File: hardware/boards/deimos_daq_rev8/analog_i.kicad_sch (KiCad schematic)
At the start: 1 part

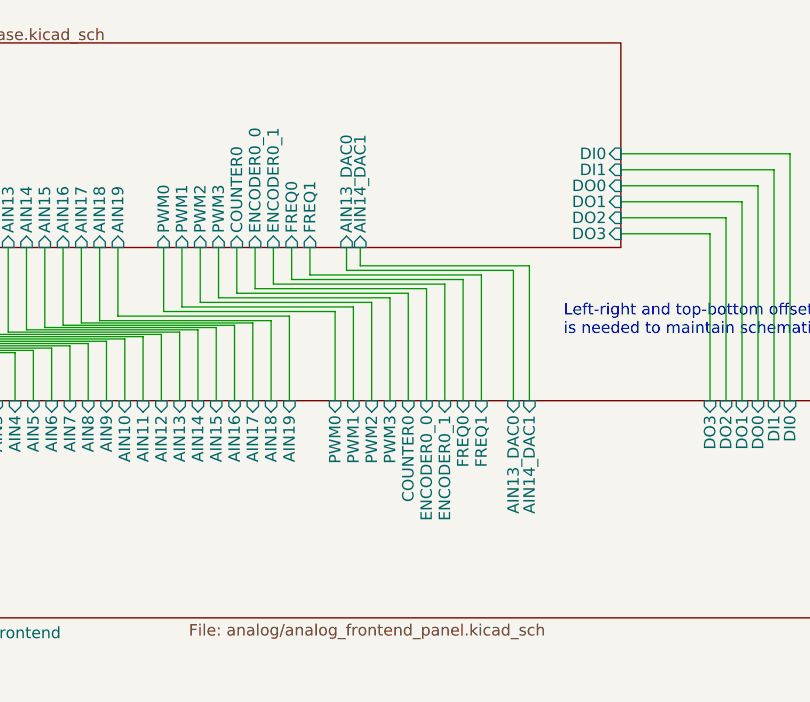
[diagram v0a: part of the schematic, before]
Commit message: update gpio input buffer schematic to use 22k resistor and schottky to 3v3 instead of zener to ground
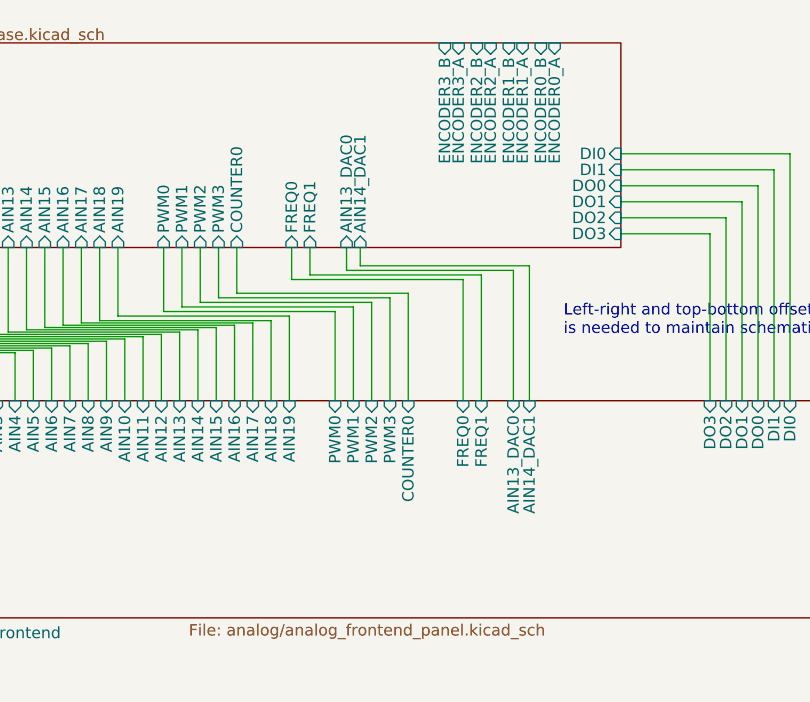
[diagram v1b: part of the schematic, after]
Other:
- sheet analog_frontend ports: added none; removed ENCODER0_0, ENCODER0_1
- sheet base ports: added ENCODER0_A, ENCODER0_B, ENCODER1_A, ENCODER1_B, ENCODER2_A, ENCODER2_B, ENCODER3_A, ENCODER3_B; removed ENCODER0_0, ENCODER0_1
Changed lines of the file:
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@@
-	(wire
-		(pts
-			(xy 71.12 39.37) (xy 71.12 43.434)
-		)
-		(stroke
-			(width 0)
-			(type default)
-		)
-	)
 	(wire
 		(pts
@@
 	(wire
 		(pts
-			(xy 71.12 43.434) (xy 90.17 43.434)
-		)
-		(stroke
-			(width 0)
-			(type default)
-		)
-	)
-	(wire
-		(pts
 			(xy 80.772 39.37) (xy 80.772 41.402)
 		)
@@
 	(wire
 		(pts
-			(xy 88.138 56.388) (xy 88.138 43.942)
-		)
-		(stroke
-			(width 0)
-			(type default)
-		)
-	)
-	(wire
-		(pts
 			(xy 77.978 56.388) (xy 77.978 46.482)
 		)
@@
 	(wire
 		(pts
-			(xy 69.088 43.942) (xy 69.088 39.37)
-		)
-		(stroke
-			(width 0)
-			(type default)
-		)
-	)
-	(wire
-		(pts
 			(xy 77.978 46.482) (xy 58.928 46.482)
 		)
@@
 	(wire
 		(pts
-			(xy 90.17 43.434) (xy 90.17 56.388)
-		)
-		(stroke
-			(width 0)
-			(type default)
-		)
-	)
-	(wire
-		(pts
 			(xy 47.752 48.006) (xy 66.802 48.006)
 		)
@@
 		(pts
 			(xy 99.568 41.402) (xy 99.568 56.388)
-		)
-		(stroke
-			(width 0)
-			(type default)
-		)
-	)
-	(wire
-		(pts
-			(xy 88.138 43.942) (xy 69.088 43.942)
 		)
 		(stroke
@@
 			)
 		)
-		(pin "ENCODER0_0" input
-			(at 69.088 39.37 270)
-			(effects
-				(font
-					(size 1.27 1.27)
-				)
-				(justify left)
-			)
-		)
-		(pin "ENCODER0_1" input
-			(at 71.12 39.37 270)
-			(effects
-				(font
-					(size 1.27 1.27)
-				)
-				(justify left)
-			)
-		)
 		(pin "FREQ0" input
 			(at 73.152 39.37 270)
@@
 		(pin "DO0" input
 			(at 109.728 32.512 0)
+			(effects
+				(font
+					(size 1.27 1.27)
+				)
+				(justify right)
+			)
+		)
+		(pin "ENCODER3_A" input
+			(at 91.694 16.637 90)
+			(effects
+				(font
+					(size 1.27 1.27)
+				)
+				(justify right)
+			)
+		)
+		(pin "ENCODER3_B" input
+			(at 90.17 16.637 90)
+			(effects
+				(font
+					(size 1.27 1.27)
+				)
+				(justify right)
+			)
+		)
+		(pin "ENCODER2_B" input
+			(at 93.726 16.637 90)
+			(effects
+				(font
+					(size 1.27 1.27)
+				)
+				(justify right)
+			)
+		)
+		(pin "ENCODER0_B" input
+			(at 100.838 16.637 90)
+			(effects
+				(font
+					(size 1.27 1.27)
+				)
+				(justify right)
+			)
+		)
+		(pin "ENCODER2_A" input
+			(at 95.25 16.637 90)
+			(effects
+				(font
+					(size 1.27 1.27)
+				)
+				(justify right)
+			)
+		)
+		(pin "ENCODER0_A" input
+			(at 102.362 16.637 90)
+			(effects
+				(font
+					(size 1.27 1.27)
+				)
+				(justify right)
+			)
+		)
+		(pin "ENCODER1_A" input
+			(at 98.806 16.637 90)
+			(effects
+				(font
+					(size 1.27 1.27)
+				)
+				(justify right)
+			)
+		)
+		(pin "ENCODER1_B" input
+			(at 97.282 16.637 90)
 			(effects
 				(font
@@
 			)
 		)
-		(pin "ENCODER0_0" input
-			(at 88.138 56.388 90)
-			(effects
-				(font
-					(size 1.27 1.27)
-				)
-				(justify right)
-			)
-		)
 		(pin "FREQ1" input
 			(at 94.234 56.388 90)
 			(effects
 				(font
-					(size 1.27 1.27)
-				)
-				(justify right)
-			)
-		)
-		(pin "ENCODER0_1" input
-			(at 90.17 56.388 90)
-			(effects
-				(font

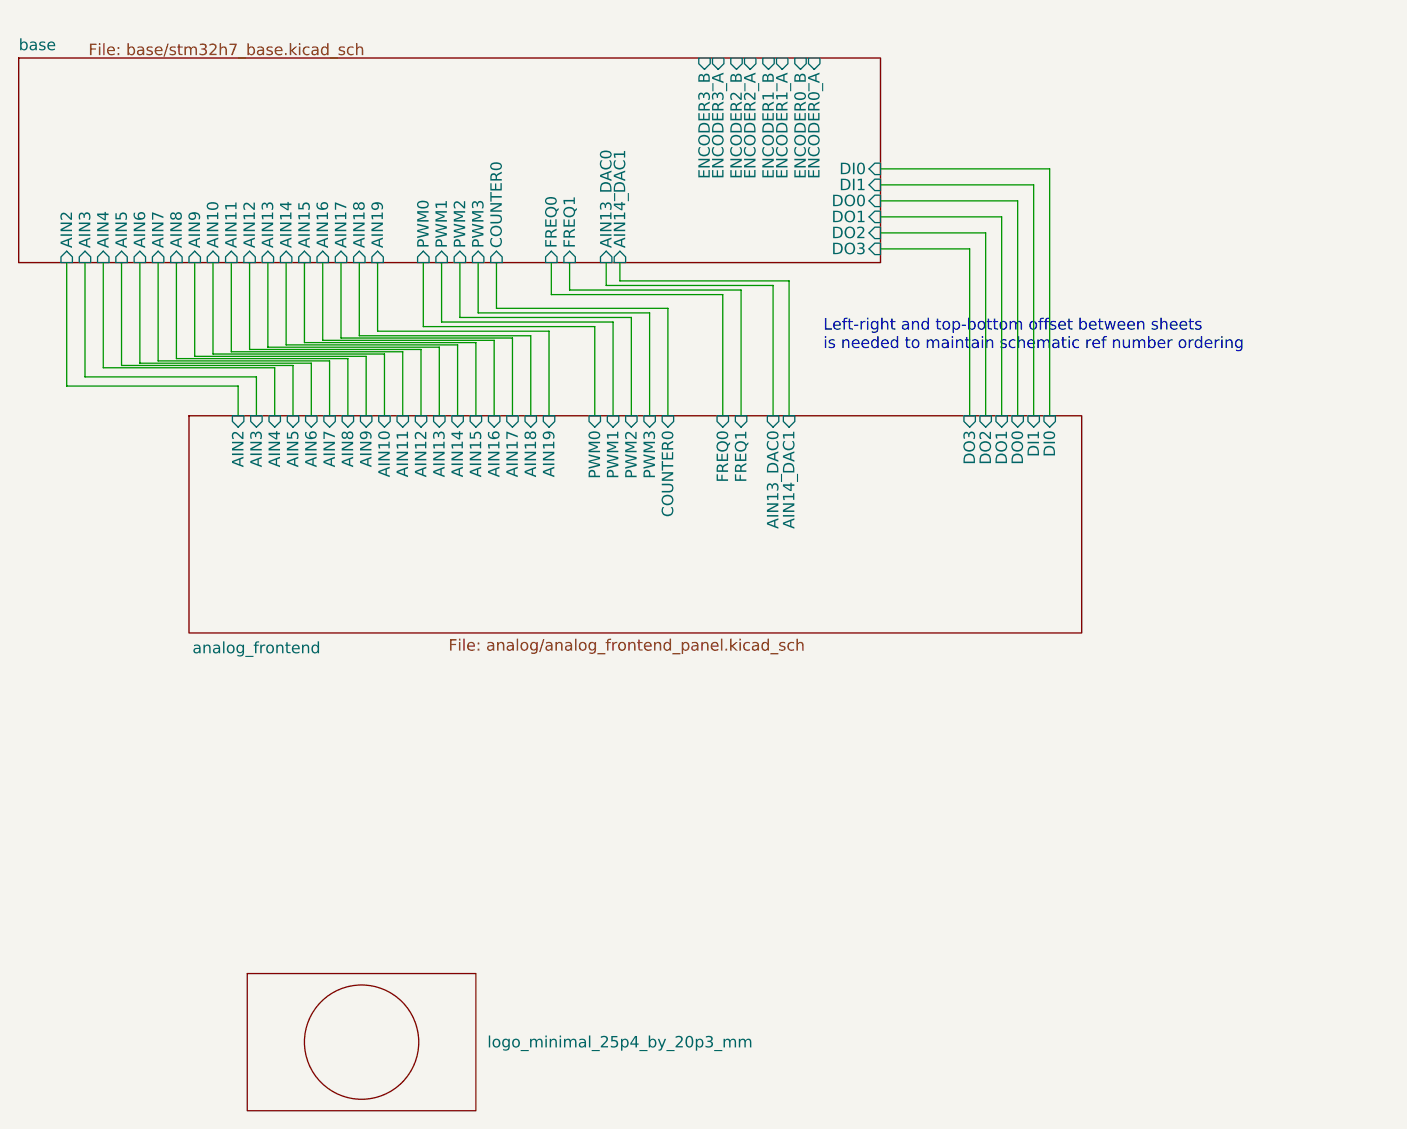
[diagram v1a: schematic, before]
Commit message: finish layout and generate fab files
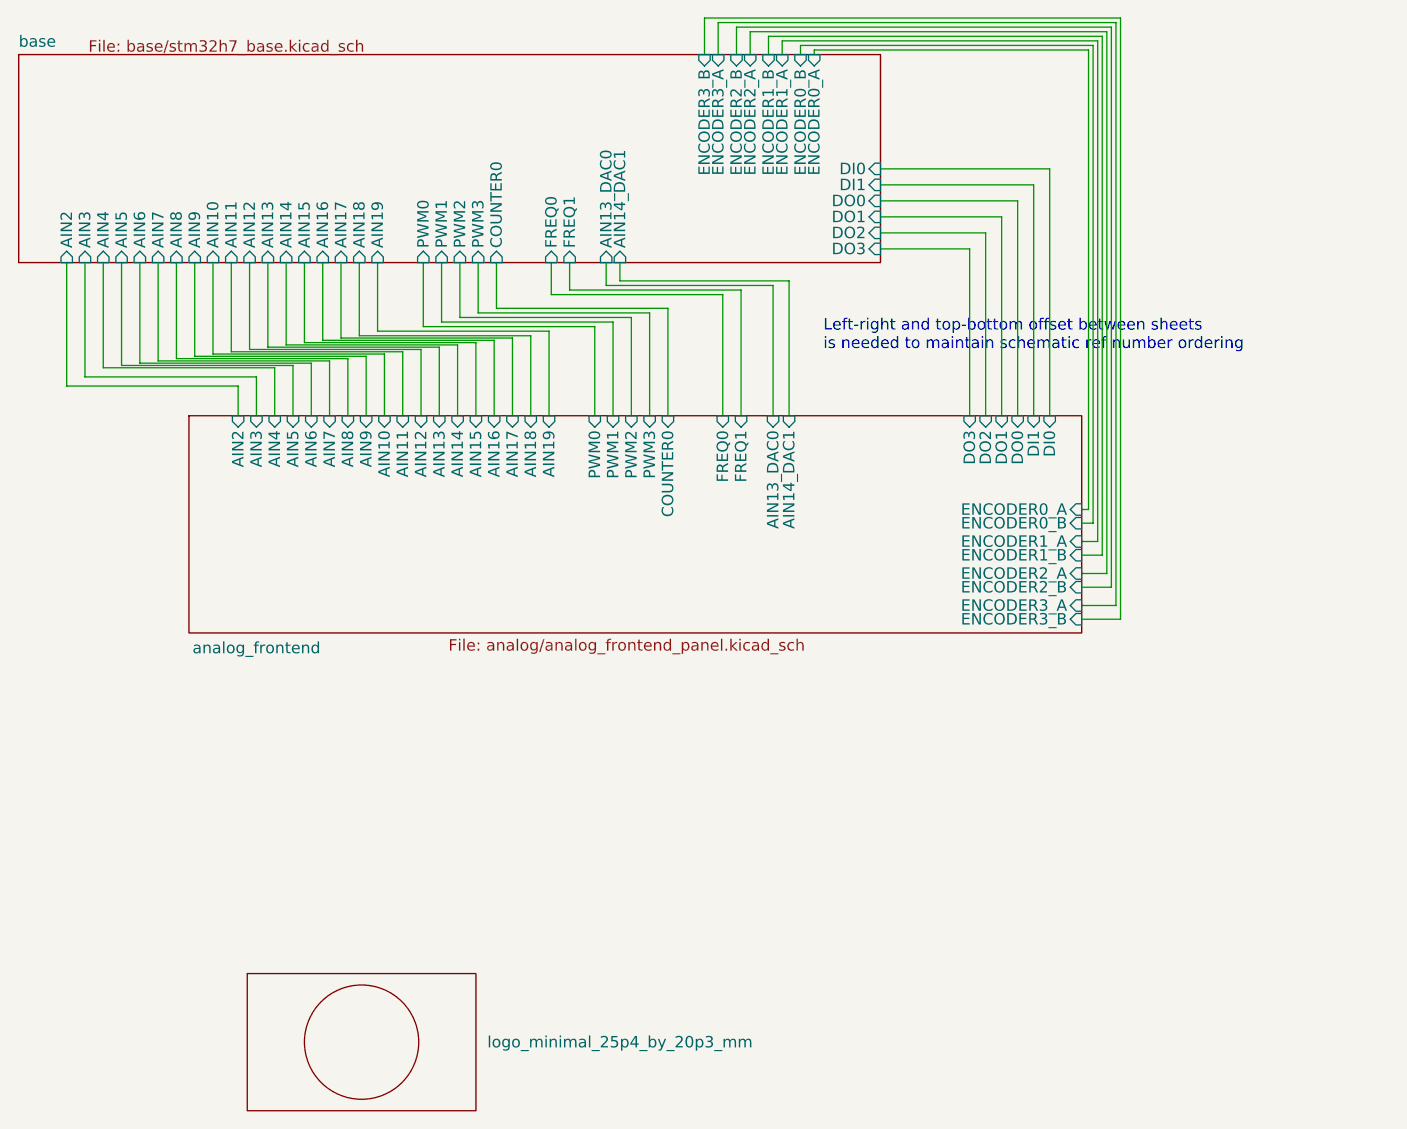
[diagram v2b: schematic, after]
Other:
- sheet analog_frontend ports: added ENCODER0_A, ENCODER0_B, ENCODER1_A, ENCODER1_B, ENCODER2_A, ENCODER2_B, ENCODER3_A, ENCODER3_B; removed none
